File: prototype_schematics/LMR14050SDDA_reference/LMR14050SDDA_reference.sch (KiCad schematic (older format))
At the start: 11 parts, among them U1 LMR14050SDDA

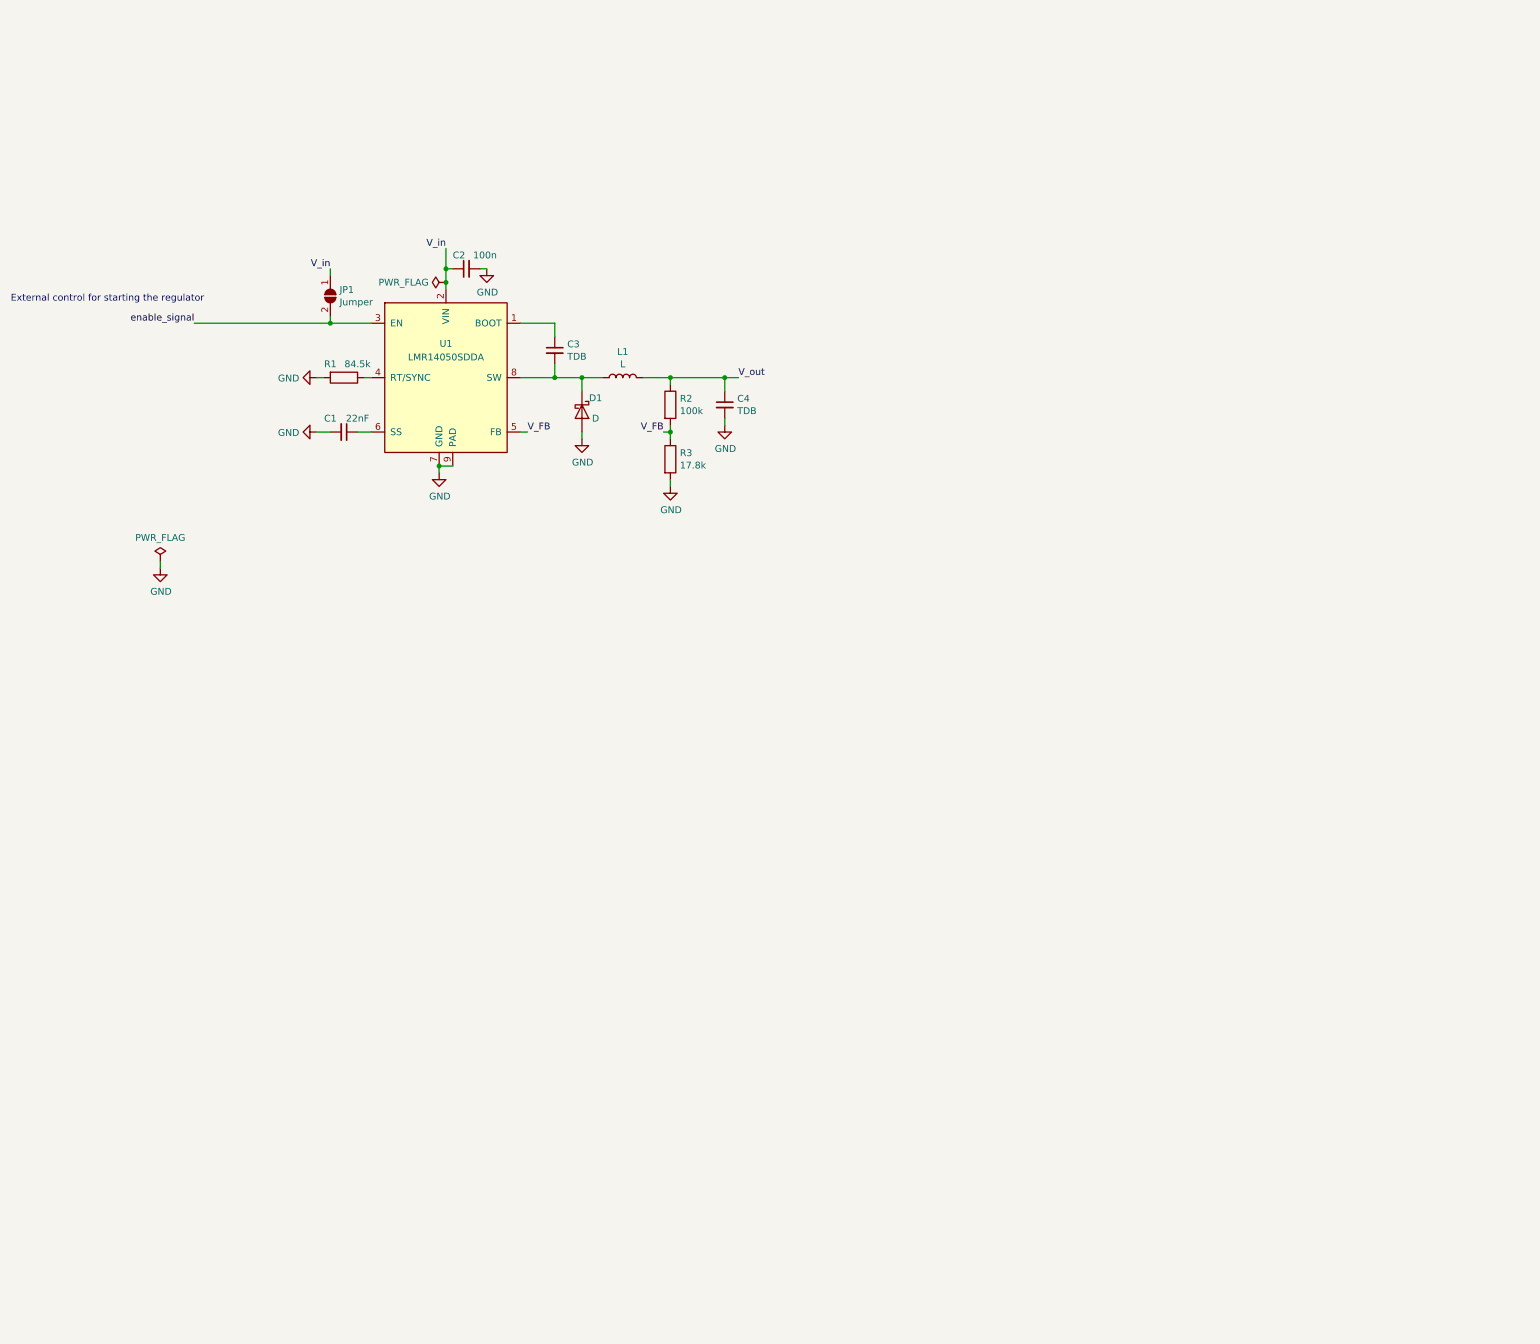
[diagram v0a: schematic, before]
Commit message: WIP Add power distribution test board rev 1.
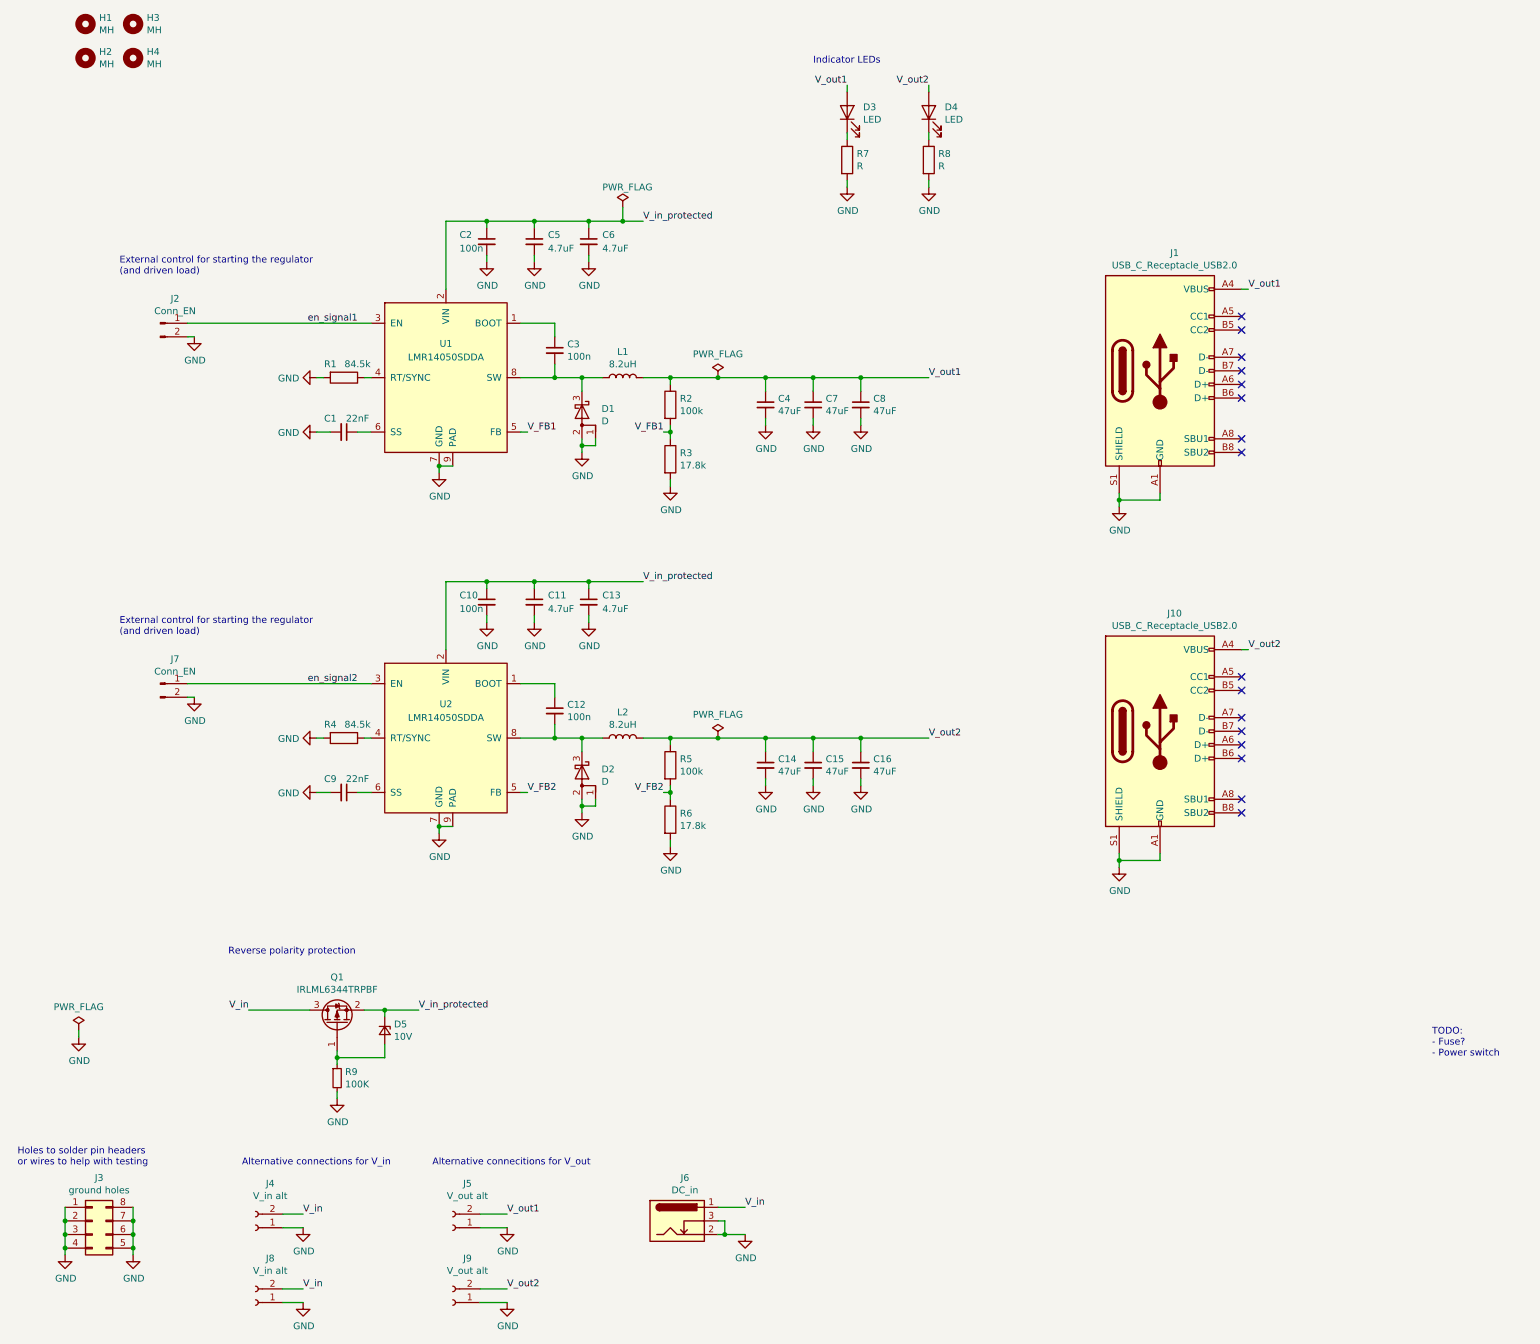
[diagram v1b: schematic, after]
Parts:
- removed D1: D, Diode_SMD:D_0603_1608Metric, symbol Device:D_Schottky
- removed JP1: Jumper, Capacitor_SMD:C_0603_1608Metric, symbol Jumper:SolderJumper_2_Open
- added C10, C12: 100n, Capacitor_SMD:C_0603_1608Metric, symbol Device:C_Small
- added C11, C13, C5, C6: 4.7uF, Capacitor_SMD:C_1206_3216Metric, symbol Device:C_Small
- added C14, C15, C16, C7, C8: 47uF, Capacitor_SMD:C_1210_3225Metric, symbol Device:C_Small
- added C9: 22nF, Capacitor_SMD:C_0603_1608Metric, symbol Device:C_Small
- added D1, D2: D, Package_TO_SOT_SMD:TO-277A, symbol Device:D_Schottky_AAK
- added D3, D4: LED, LED_SMD:LED_0805_2012Metric, symbol Device:LED
- added D5: 10V, Diode_SMD:D_SOD-323, symbol Device:D_Zener_Small
- added H1, H2, H3, H4: MH, MountingHole:MountingHole_3.2mm_M3, symbol Mechanical:MountingHole
- added J1, J10: USB_C_Receptacle_USB2.0, Connector_USB:USB_C_Receptacle_GCT_USB4085, symbol Connector:USB_C_Receptacle_USB2.0
- added J2, J7: Conn_EN, Connector_PinHeader_2.54mm:PinHeader_1x02_P2.54mm_Vertical, symbol Connector:Conn_01x02_Male
- added J3: ground holes, Connector_PinHeader_2.54mm:PinHeader_2x04_P2.54mm_Vertical, symbol Connector_Generic:Conn_02x04_Counter_Clockwise
- added J4, J8: V_in alt, TerminalBlock:TerminalBlock_bornier-2_P5.08mm, symbol Connector:Conn_01x02_Female
- added J5, J9: V_out alt, TerminalBlock:TerminalBlock_bornier-2_P5.08mm, symbol Connector:Conn_01x02_Female
- added J6: DC_in, Connector_BarrelJack:BarrelJack_Wuerth_6941xx301002, symbol Connector:Barrel_Jack_Switch
- added L2: 8.2uH, Inductor_SMD:L_Wuerth_WE-PD-Typ-LS, symbol Device:L
- added Q1: IRLML6344TRPBF, Package_TO_SOT_SMD:SOT-23, symbol Transistor_FET:IRLML9301
- added R4: 84.5k, Resistor_SMD:R_0603_1608Metric, symbol Device:R
- added R5: 100k, Resistor_SMD:R_0603_1608Metric, symbol Device:R
- added R6: 17.8k, Resistor_SMD:R_0603_1608Metric, symbol Device:R
- added R7, R8: R, Resistor_SMD:R_0805_2012Metric, symbol Device:R
- added R9: 100K, Resistor_SMD:R_0603_1608Metric, symbol Device:R_Small
- added U2: LMR14050SDDA, Package_SO:Texas_HSOP-8-1EP_3.9x4.9mm_P1.27mm_ThermalVias, symbol LMR14050:LMR14050SDDA
- C3: value TDB -> 100n
- C4: value TDB -> 47uF; footprint Capacitor_SMD:C_0603_1608Metric -> Capacitor_SMD:C_1210_3225Metric
- L1: value L -> 8.2uH; footprint Inductor_SMD:L_0603_1608Metric -> Inductor_SMD:L_Wuerth_WE-PD-Typ-LS
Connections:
- net GND: now also C10.2, C11.2, C13.2, C14.2, C15.2, C16.2, C5.2, C6.2, C7.2, C8.2, C9.2, D1.1 (A), D1.2 (A), D2.1 (A), D2.2 (A), J1.A1 (GND), J1.A12 (GND), J1.B1 (GND), J1.B12 (GND), J1.S1 (SHIELD), J10.A1 (GND), J10.A12 (GND), J10.B1 (GND), J10.B12 (GND), J10.S1 (SHIELD), J2.2 (Pin_2), J3.1 (Pin_1), J3.2 (Pin_2), J3.3 (Pin_3), J3.4 (Pin_4), J3.5 (Pin_5), J3.6 (Pin_6), J3.7 (Pin_7), J3.8 (Pin_8), J4.1 (Pin_1), J5.1 (Pin_1), J6.2, J6.3, J7.2 (Pin_2), J8.1 (Pin_1), J9.1 (Pin_1), R4.2, R6.2, R7.2, R8.2, R9.2, U2.7 (GND), U2.9 (PAD)
- net V_in: now also J4.2 (Pin_2), J6.1, J8.2 (Pin_2), Q1.3 (D); no longer C2.1, U1.2 (VIN)
- net at C3.2, L1.1, U1.8 (SW): now also D1.3 (K)
- net V_FB renamed V_FB1
- net V_out renamed V_out1
- net V_out1: now also C7.1, C8.1, D3.2 (A), J1.A4 (VBUS), J1.A9 (VBUS), J1.B4 (VBUS), J1.B9 (VBUS), J5.2 (Pin_2)
- net enable_signal renamed en_signal1
- net en_signal1: now also J2.1 (Pin_1)
- new net: D5.2 (A), Q1.1 (G), R9.1
- new net: C12.1, U2.1 (BOOT)
- new net: R4.1, U2.4 (RT/SYNC)
- new net: C9.1, U2.6 (SS)
- new net: C12.2, D2.3 (K), L2.1, U2.8 (SW)
- new net: D3.1 (K), R7.1
- new net: D4.1 (K), R8.1
- new net V_FB2: R5.2, R6.1, U2.5 (FB)
- new net V_in_protected: C10.1, C11.1, C13.1, C2.1, C5.1, C6.1, D5.1 (K), Q1.2 (S), U1.2 (VIN), U2.2 (VIN)
- new net V_out2: C14.1, C15.1, C16.1, D4.2 (A), J10.A4 (VBUS), J10.A9 (VBUS), J10.B4 (VBUS), J10.B9 (VBUS), J9.2 (Pin_2), L2.2, R5.1
- new net en_signal2: J7.1 (Pin_1), U2.3 (EN)
- no-connect marks 0 -> 16
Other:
- note added: "Alternative connecitions for V_out"
- note added: "Alternative connections for V_in"
- note added: "External control for starting the regulator\n(and driven load)\n"
- note added: "Holes to solder pin headers\nor wires to help with testing"
- note added: "Indicator LEDs"
- note added: "Reverse polarity protection"
- note added: "TODO:\n- Fuse?\n- Power switch"
- note removed: "External control for starting the regulator\n"
- moved on the sheet: C2, C4
